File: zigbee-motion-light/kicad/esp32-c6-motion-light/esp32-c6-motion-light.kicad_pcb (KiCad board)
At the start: 4 copper layers, 26.8 x 35 mm, 2 parts, among them U1 XIAO-ESP32-C6-DIP

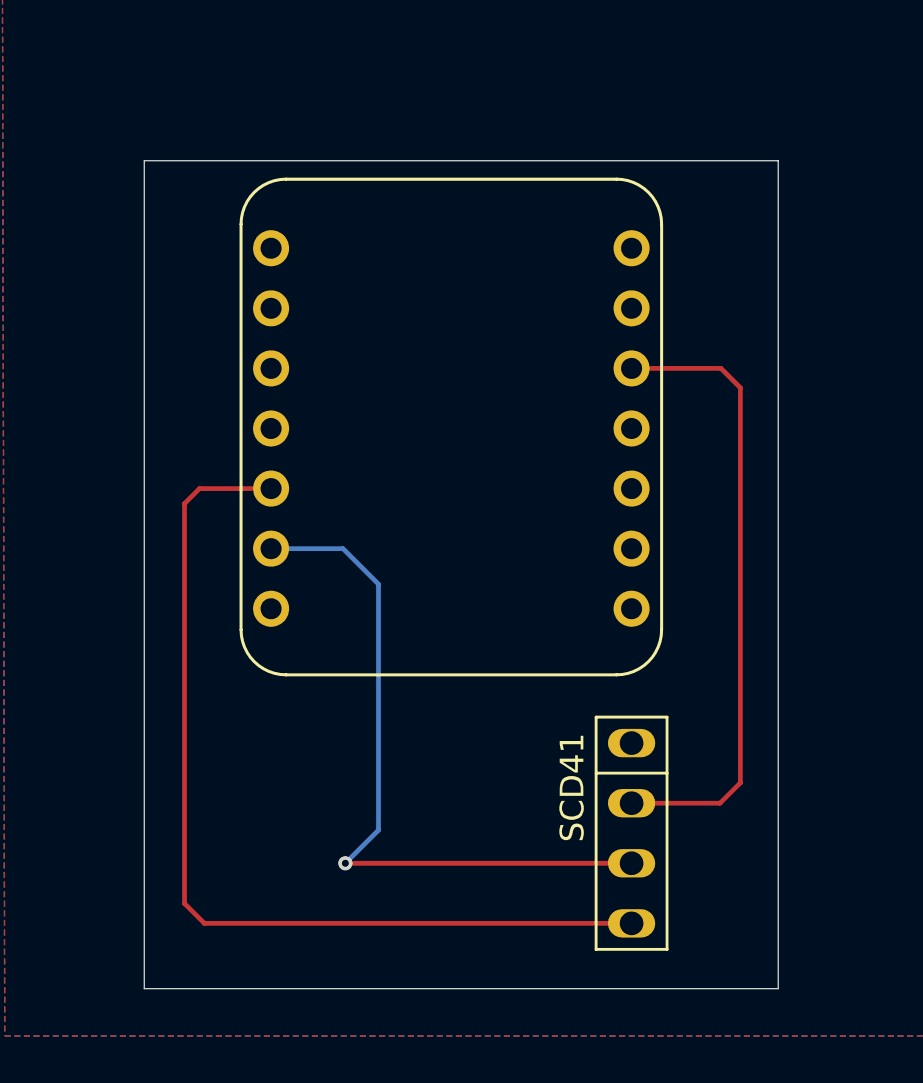
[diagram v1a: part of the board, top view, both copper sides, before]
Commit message: Remove unused custom KiCAD footprints (SCD41-4pins and XIAO-ESP32-C6-DIP)
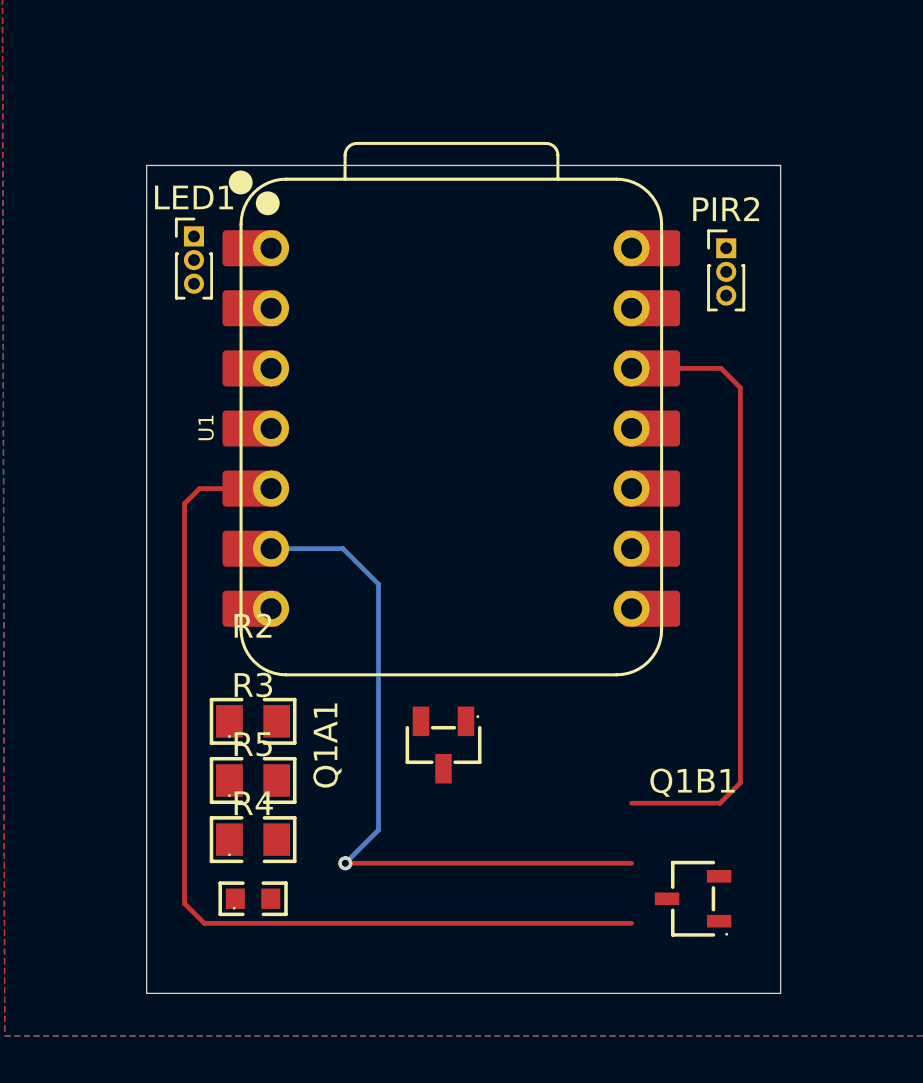
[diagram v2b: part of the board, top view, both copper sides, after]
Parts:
- removed SCD41: ~, Library:SCD41-4pins
- added LED1: ~, Connector_PinHeader_1.00mm:PinHeader_1x03_P1.00mm_Vertical, F.Cu at (60.5, 42.5)
- added PIR2: ~, Connector_PinHeader_1.00mm:PinHeader_1x03_P1.00mm_Vertical, F.Cu at (83.0, 43.0)
- added Q1A1: 2N7002, 1_easyeda2kicad:SOT-23-3_L2.9-W1.3-P1.90-LS2.4-BR, F.Cu at (71.0, 64.0)
- added Q1B1: BSS84, 1_easyeda2kicad:SOT-23-3_L3.0-W1.7-P0.95-LS2.9-BR, F.Cu at (81.6, 70.5)
- added R2: 1M0, 1_easyeda2kicad:R0805, F.Cu at (63.0, 63.0)
- added R3: 1M0, 1_easyeda2kicad:R0805, F.Cu at (63.0, 65.5)
- added R4: 1M5, 1_easyeda2kicad:R0603, F.Cu at (63.0, 70.5)
- added R5: 220K, 1_easyeda2kicad:R0805, F.Cu at (63.0, 68.0)
- U1: footprint Library:XIAO-ESP32-C6-DIP -> 1_seeds-studio:XIAO-ESP32-S3-DIP
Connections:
- U1 pad 1: unconnected-(U1-GPIO0/A0/D0-Pad1) -> /BATTERY_MONITORING
- U1 pad 2: unconnected-(U1-GPIO1/A1/D1-Pad2) -> /BATTERY_MONITORING_ENABLER
- U1 pad 3: unconnected-(U1-GPIO2/A2/D2-Pad3) -> /PIR_SENSOR
- U1 pad 4: unconnected-(U1-GPIO21/D3-Pad4) -> /LED_CONTROL
- U1 pad 5: Net-(SCD41-SDA) -> unconnected-(U1-GPIO22/D4/SDA-Pad5)_1
- U1 pad 6: Net-(SCD41-SCL) -> unconnected-(U1-GPIO23/D5/SCL-Pad6)_1
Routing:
- net unconnected-(U1-GPIO23/D5/SCL-Pad6)_1: track 0.00 -> 29.6 mm, vias 0 -> 1
- net Net-(SCD41-SCL): track 29.6 -> 0.00 mm, vias 1 -> 0

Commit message: feat: update kikad
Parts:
- added J1: Conn_01x02, Connector_JST:JST_XH_B2B-XH-A_1x02_P2.50mm_Vertical, F.Cu at (127.0, 62.0)
- added JP1: Enabled for Batter Monitoring, Jumper:SolderJumper-2_P1.3mm_Open_RoundedPad1.0x1.5mm, F.Cu at (119.8, 64.5)
- added TP1: GND, TestPoint:TestPoint_Pad_2.0x2.0mm, F.Cu at (129.0, 30.0)
- added TP2: BATT+, TestPoint:TestPoint_Pad_2.0x2.0mm, F.Cu at (129.0, 45.5)
- added TP3: BATT-, TestPoint:TestPoint_Pad_2.0x2.0mm, F.Cu at (129.0, 51.5)
- added TP4: +3.3, TestPoint:TestPoint_Pad_2.0x2.0mm, F.Cu at (129.0, 36.0)
- moved LED1 113.3 mm to (116.5, 141.0), turned to -90 degrees
- moved R2 49.6 mm to (112.5, 66.4), turned to 90 degrees
- moved R3 49.0 mm to (111.0, 55.5), turned to -90 degrees
- moved R4 43.9 mm to (106.0, 61.6), turned to -90 degrees
- moved U1 43.7 mm to (113.4, 38.6)
- moved R5 43.0 mm to (106.0, 66.4), turned to -90 degrees
- moved Q1A1 40.5 mm to (111.5, 61.5), turned to 0 degrees
- moved PIR2 39.0 mm to (119.0, 58.0)
- moved Q1B1 27.6 mm to (106.0, 57.8), turned to 90 degrees
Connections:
- net +BATT renamed Net-(JP1-A)
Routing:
- net +3.3V: track 25.8 -> 159.7 mm, vias 0 -> 2
- net /LED_CONTROL: track 0.00 -> 124.0 mm, vias 0 -> 2
- net /BATTERY_MONITORING: track 0.00 -> 42.5 mm
- net /BATTERY_MONITORING_ENABLER: track 0.00 -> 41.3 mm, vias 0 -> 2
- net Net-(SCD41-SDA): track 39.2 -> 0.00 mm
- net /PIR_SENSOR: track 0.00 -> 34.8 mm
- net Net-(JP1-A): track 0.00 -> 33.2 mm
- net +BATT: track 0.00 -> 31.6 mm
- net unconnected-(U1-GPIO23/D5/SCL-Pad6): track 29.6 -> 0.00 mm, vias 1 -> 0
- net -BATT: track 0.00 -> 12.2 mm
- net Net-(Q1A1-D): track 0.00 -> 10.3 mm
- net Net-(Q1B1-D): track 0.00 -> 2.02 mm
- removed copper zone on In1.Cu, net GND
- removed copper zone on In2.Cu, net GND
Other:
- board size 26.8 x 35 mm -> 33 x 118 mm

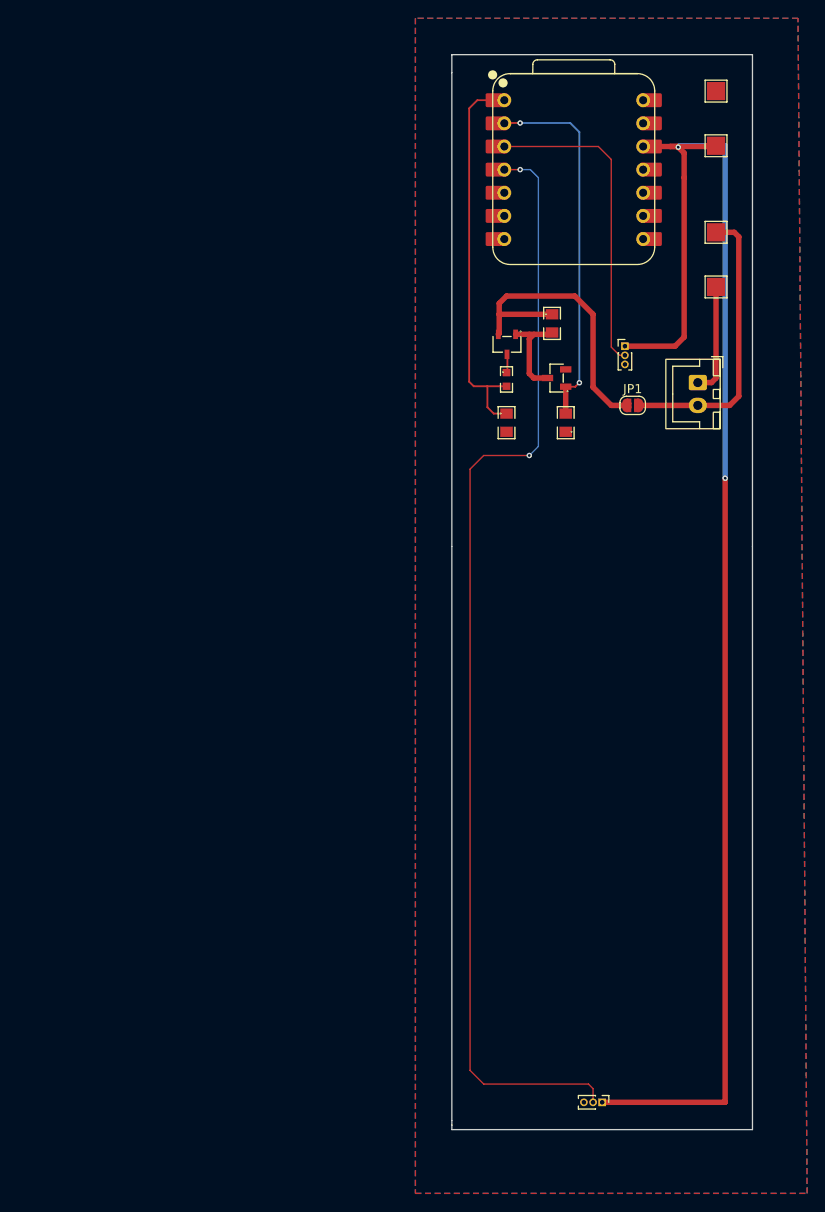
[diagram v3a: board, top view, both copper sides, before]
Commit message: fix: wait for Zigbee join before deep sleep and fix task lifecycle
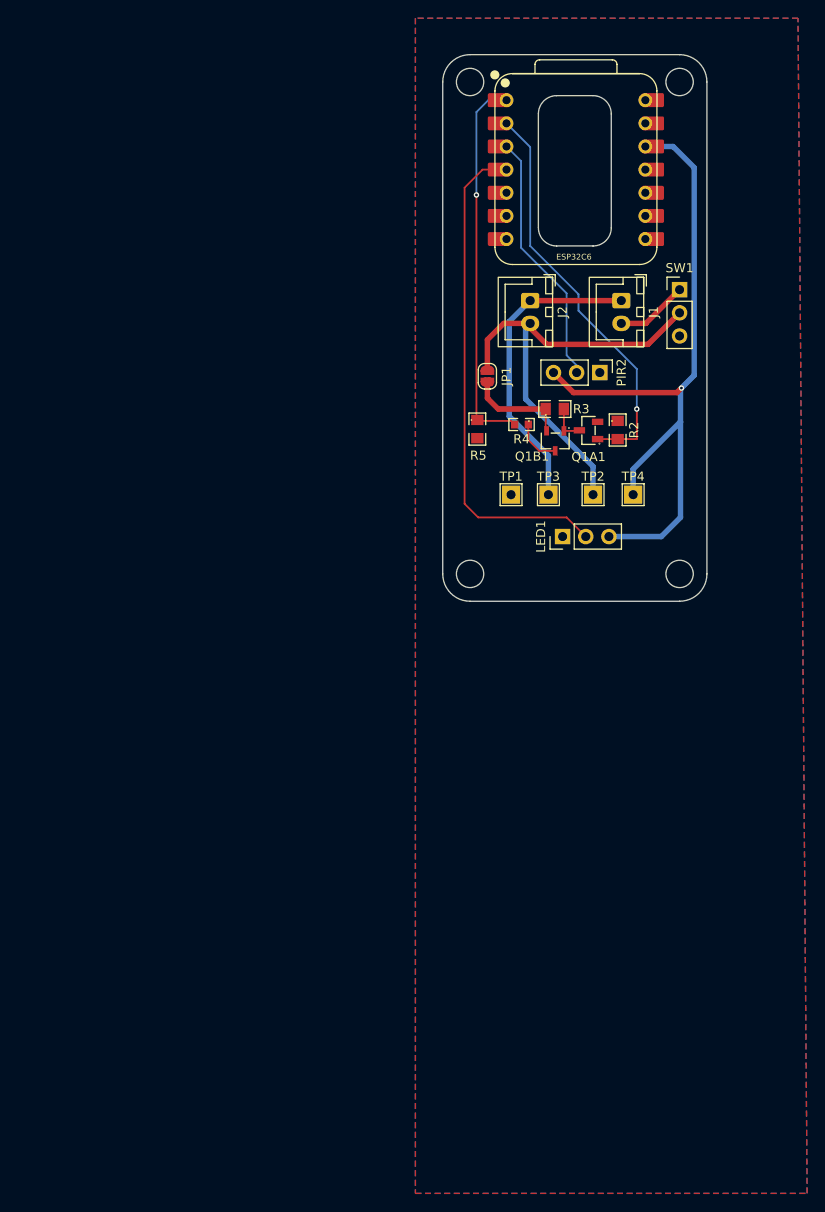
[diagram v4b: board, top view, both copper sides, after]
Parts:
- added J2: Conn_01x02, Connector_JST:JST_XH_B2B-XH-A_1x02_P2.50mm_Vertical, F.Cu at (108.6, 53.0)
- added SW1: SW_SPST, Connector_PinHeader_2.54mm:PinHeader_1x03_P2.54mm_Vertical, F.Cu at (125.0, 51.8)
- LED1, PIR2: footprint Connector_PinHeader_1.00mm:PinHeader_1x03_P1.00mm_Vertical -> Connector_PinHeader_2.54mm:PinHeader_1x03_P2.54mm_Vertical
- TP1, TP2, TP3, TP4: footprint TestPoint:TestPoint_Pad_2.0x2.0mm -> TestPoint:TestPoint_THTPad_2.0x2.0mm_Drill1.0mm
- moved LED1 62.3 mm to (112.2, 78.9), turned to 90 degrees
- moved TP1 49.7 mm to (106.5, 74.3)
- moved TP4 39.4 mm to (119.9, 74.3)
- moved TP2 31.8 mm to (115.5, 74.3)
- moved TP3 29.3 mm to (110.6, 74.3)
- moved JP1 16.3 mm to (103.9, 61.3), turned to 90 degrees
- moved J1 12.3 mm to (118.6, 53.0)
- moved Q1B1 11.9 mm to (111.3, 68.4)
- moved R3 9.40 mm to (111.3, 64.9), turned to 0 degrees
- moved Q1A1 6.73 mm to (115.0, 67.2)
- moved R2 5.76 mm to (118.2, 67.2), turned to -90 degrees
- moved R4 5.22 mm to (107.7, 66.6), turned to 180 degrees
- moved PIR2 4.00 mm to (116.2, 60.9), turned to -90 degrees
- moved R5 3.28 mm to (102.8, 67.1)
- moved ESP32C6 0.24 mm to (113.6, 38.6)
- renumbered U1 to ESP32C6
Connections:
- J1 pad 2: +BATT -> Net-(J1-Pin_2)
- LED1 pad 1: +3.3V -> GND
- LED1 pad 3: GND -> +3.3V
- PIR2 pad 1: +3.3V -> GND
- PIR2 pad 3: GND -> +3.3V
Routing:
- net +3.3V: track 159.7 -> 79.5 mm, vias 2 -> 1
- net /LED_CONTROL: track 124.0 -> 54.1 mm, vias 2 -> 0
- net Net-(JP1-A): track 33.2 -> 11.1 mm
- net -BATT: track 12.2 -> 34.0 mm
- net +BATT: track 31.6 -> 49.9 mm
- net Net-(J1-Pin_2): track 0.00 -> 7.93 mm
- net /PIR_SENSOR: track 34.8 -> 28.0 mm
- net Net-(Q1A1-D): track 10.3 -> 4.12 mm
- net /BATTERY_MONITORING_ENABLER: track 41.3 -> 45.3 mm, vias 2 -> 1
- net Net-(Q1B1-D): track 2.02 -> 5.15 mm
- net /BATTERY_MONITORING: track 42.5 -> 41.4 mm, vias 0 -> 1
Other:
- board size 33 x 118 mm -> 29 x 60 mm

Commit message: update KiCAD files
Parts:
- added G***: LOGO, LOGO, F.Cu at (104.0, 79.5)
- moved TP1 16.0 mm to (122.5, 74.3)
- moved PIR2 3.78 mm to (112.5, 60.9), turned to 90 degrees
- moved JP1 2.62 mm to (106.5, 61.0)
- moved TP4 1.40 mm to (118.5, 74.3)
- moved TP2 1.00 mm to (114.5, 74.3)
- moved R5 0.40 mm to (102.8, 67.5)
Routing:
- net +3.3V: track 79.5 -> 68.3 mm
- net Net-(JP1-A): track 11.1 -> 8.96 mm
- net +BATT: track 49.9 -> 48.0 mm
- net /PIR_SENSOR: track 28.0 -> 28.5 mm
- net /BATTERY_MONITORING: track 41.4 -> 41.9 mm
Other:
- board size 29 x 60 mm -> 29 x 58 mm
- board text added: "JLCJLCJLCJLC"
- board text added: "Motion Sensor v.1.0.0"
